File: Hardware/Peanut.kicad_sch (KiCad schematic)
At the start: 4 parts, among them J1 Conn_02x04_Odd_Even, J2 Conn_02x04_Odd_Even, SW6 Slide Switch

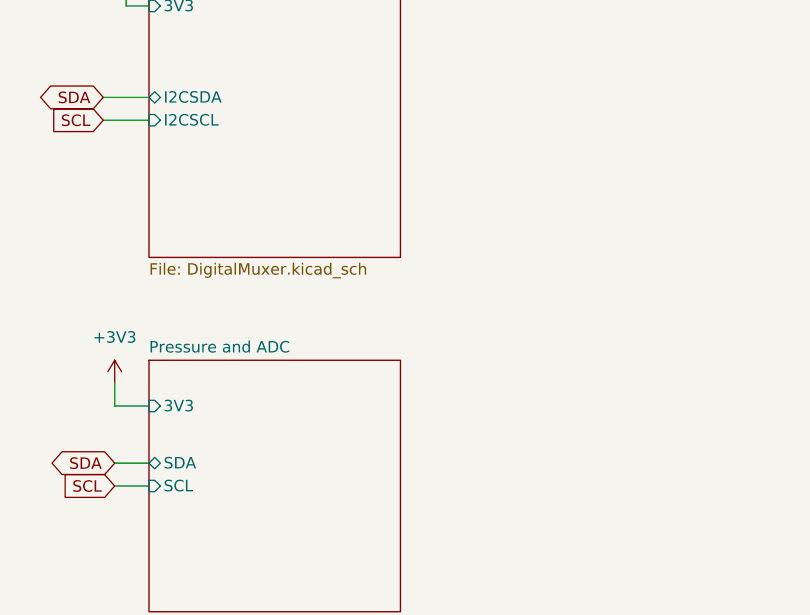
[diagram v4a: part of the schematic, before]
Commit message: Replace 1 LED with battery measurement toggle - We require an additional IO to toggle battery draining for % measurement, however we had no more ports. After a group discussion, one LED was dropped.
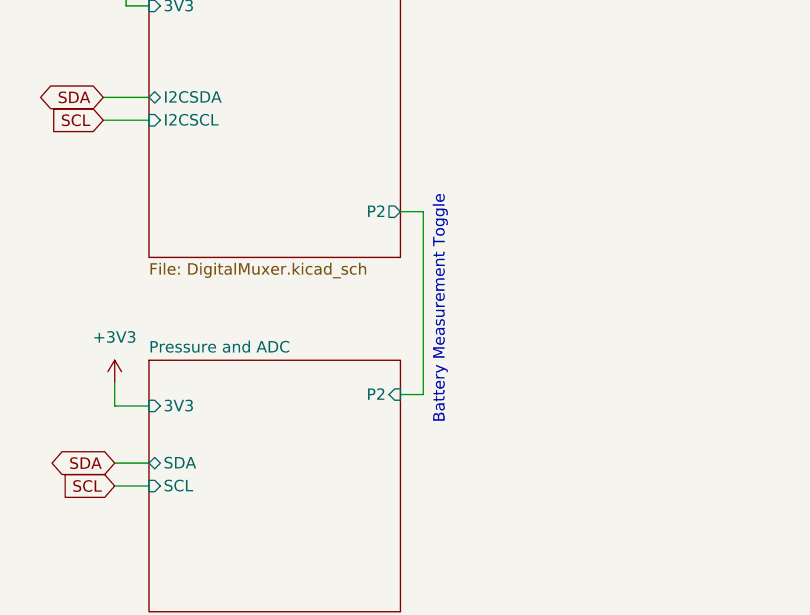
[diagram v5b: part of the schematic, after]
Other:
- sheet DigitalMuxer ports: added P2; removed none
- sheet Pressure and ADC ports: added P2; removed none
- note added: "Battery Measurement Toggle"
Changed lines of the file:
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@@
+	(wire
+		(pts
+			(xy 165.1 132.08) (xy 165.1 152.4)
+		)
+		(stroke
+			(width 0)
+			(type default)
+		)
+	)
 	(wire
 		(pts
@@
 	(wire
 		(pts
+			(xy 162.56 132.08) (xy 165.1 132.08)
+		)
+		(stroke
+			(width 0)
+			(type default)
+		)
+	)
+	(wire
+		(pts
 			(xy 175.26 38.1) (xy 177.8 38.1)
+		)
+		(stroke
+			(width 0)
+			(type default)
+		)
+	)
+	(wire
+		(pts
+			(xy 165.1 152.4) (xy 162.56 152.4)
 		)
 		(stroke
@@
 		(exclude_from_sim no)
 		(at 125.73 34.29 0)
+		(effects
+			(font
+				(size 1.27 1.27)
+			)
+		)
+	)
+	(text "Battery Measurement Toggle"
+		(exclude_from_sim no)
+		(at 166.878 143.002 90)
 		(effects
 			(font
@@
 			)
 		)
+		(pin "P2" output
+			(at 162.56 132.08 0)
+			(effects
+				(font
+					(size 1.27 1.27)
+				)
+				(justify right)
+			)
+		)
 		(instances
 			(project "Peanut"
@@
 			)
 		)
+		(pin "P2" input
+			(at 162.56 152.4 0)
+			(effects
+				(font
+					(size 1.27 1.27)
+				)
+				(justify right)
+			)
+		)

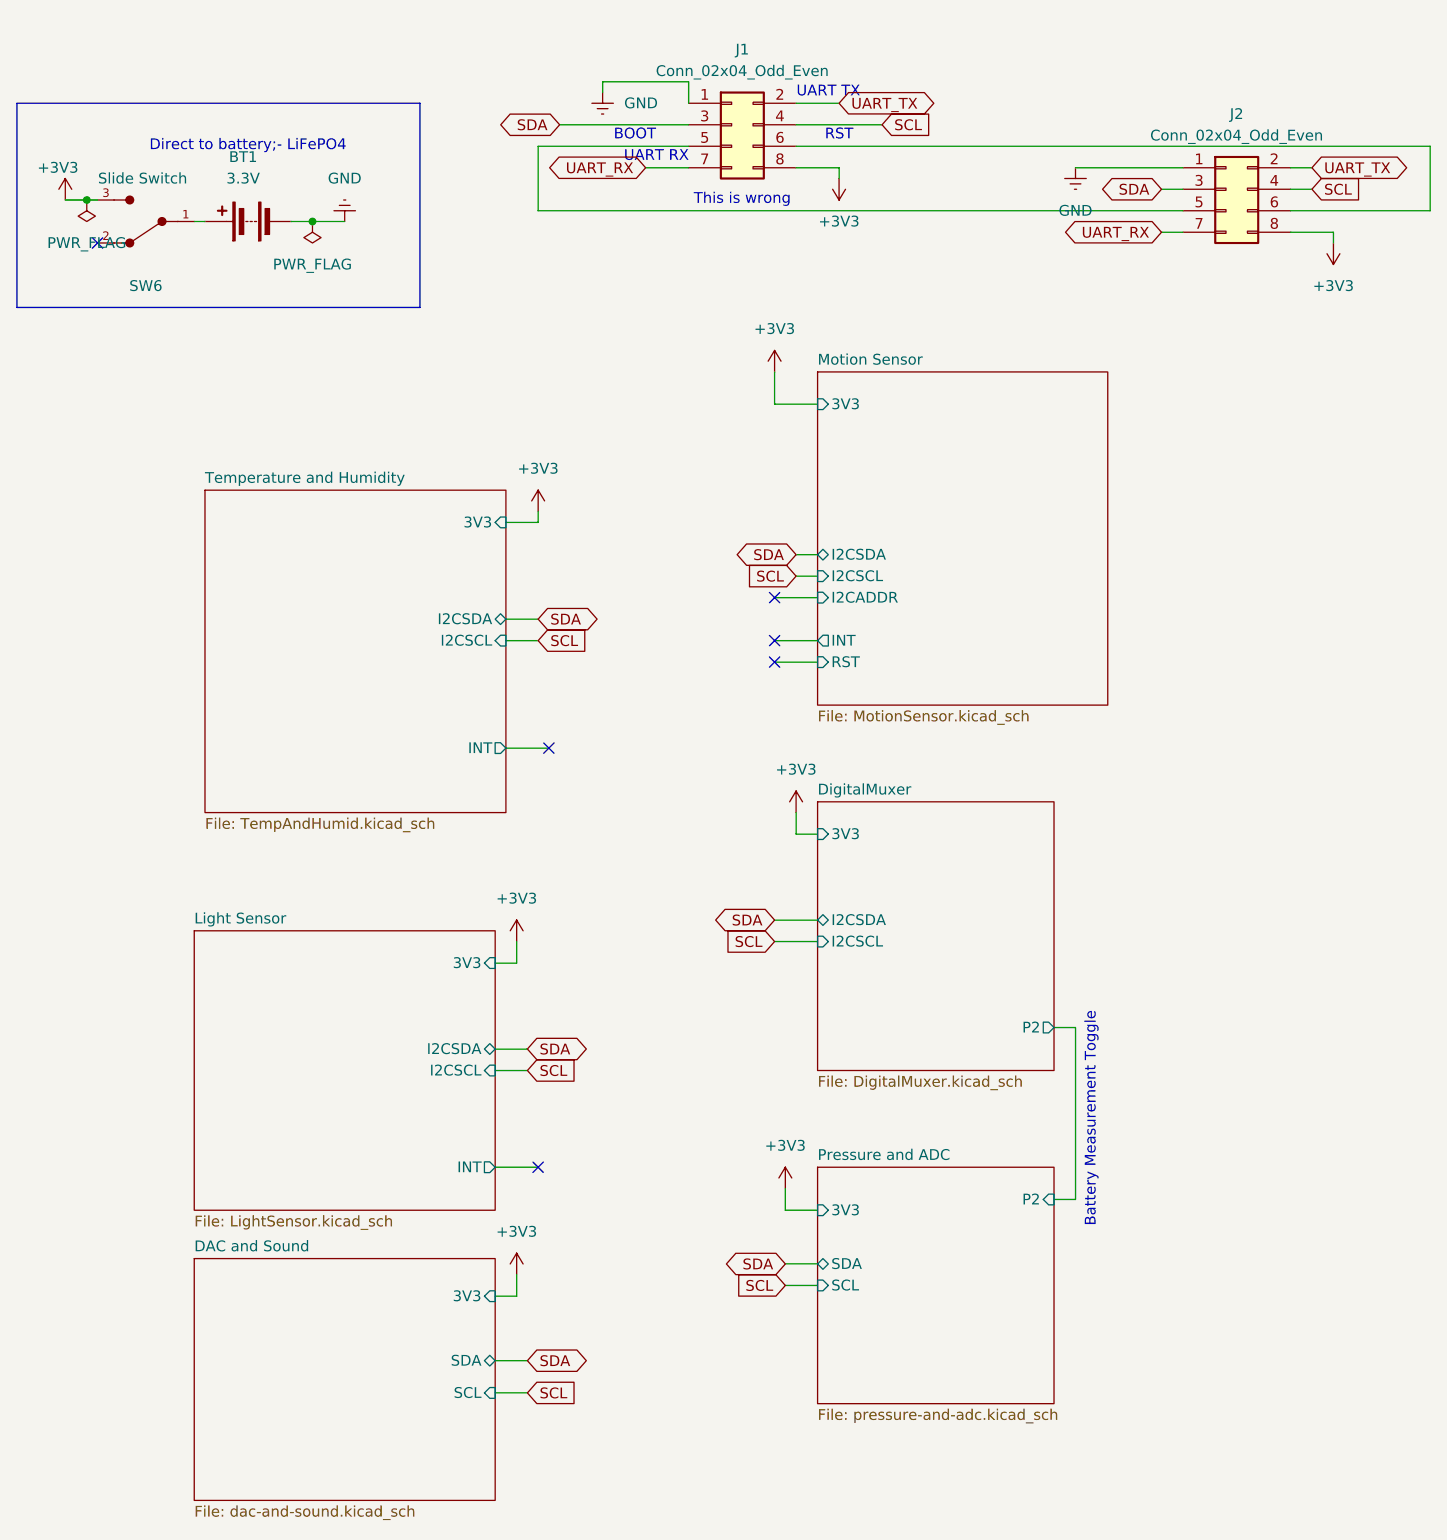
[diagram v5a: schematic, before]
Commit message: Add Battery Monitoring & Use Project Parts Library
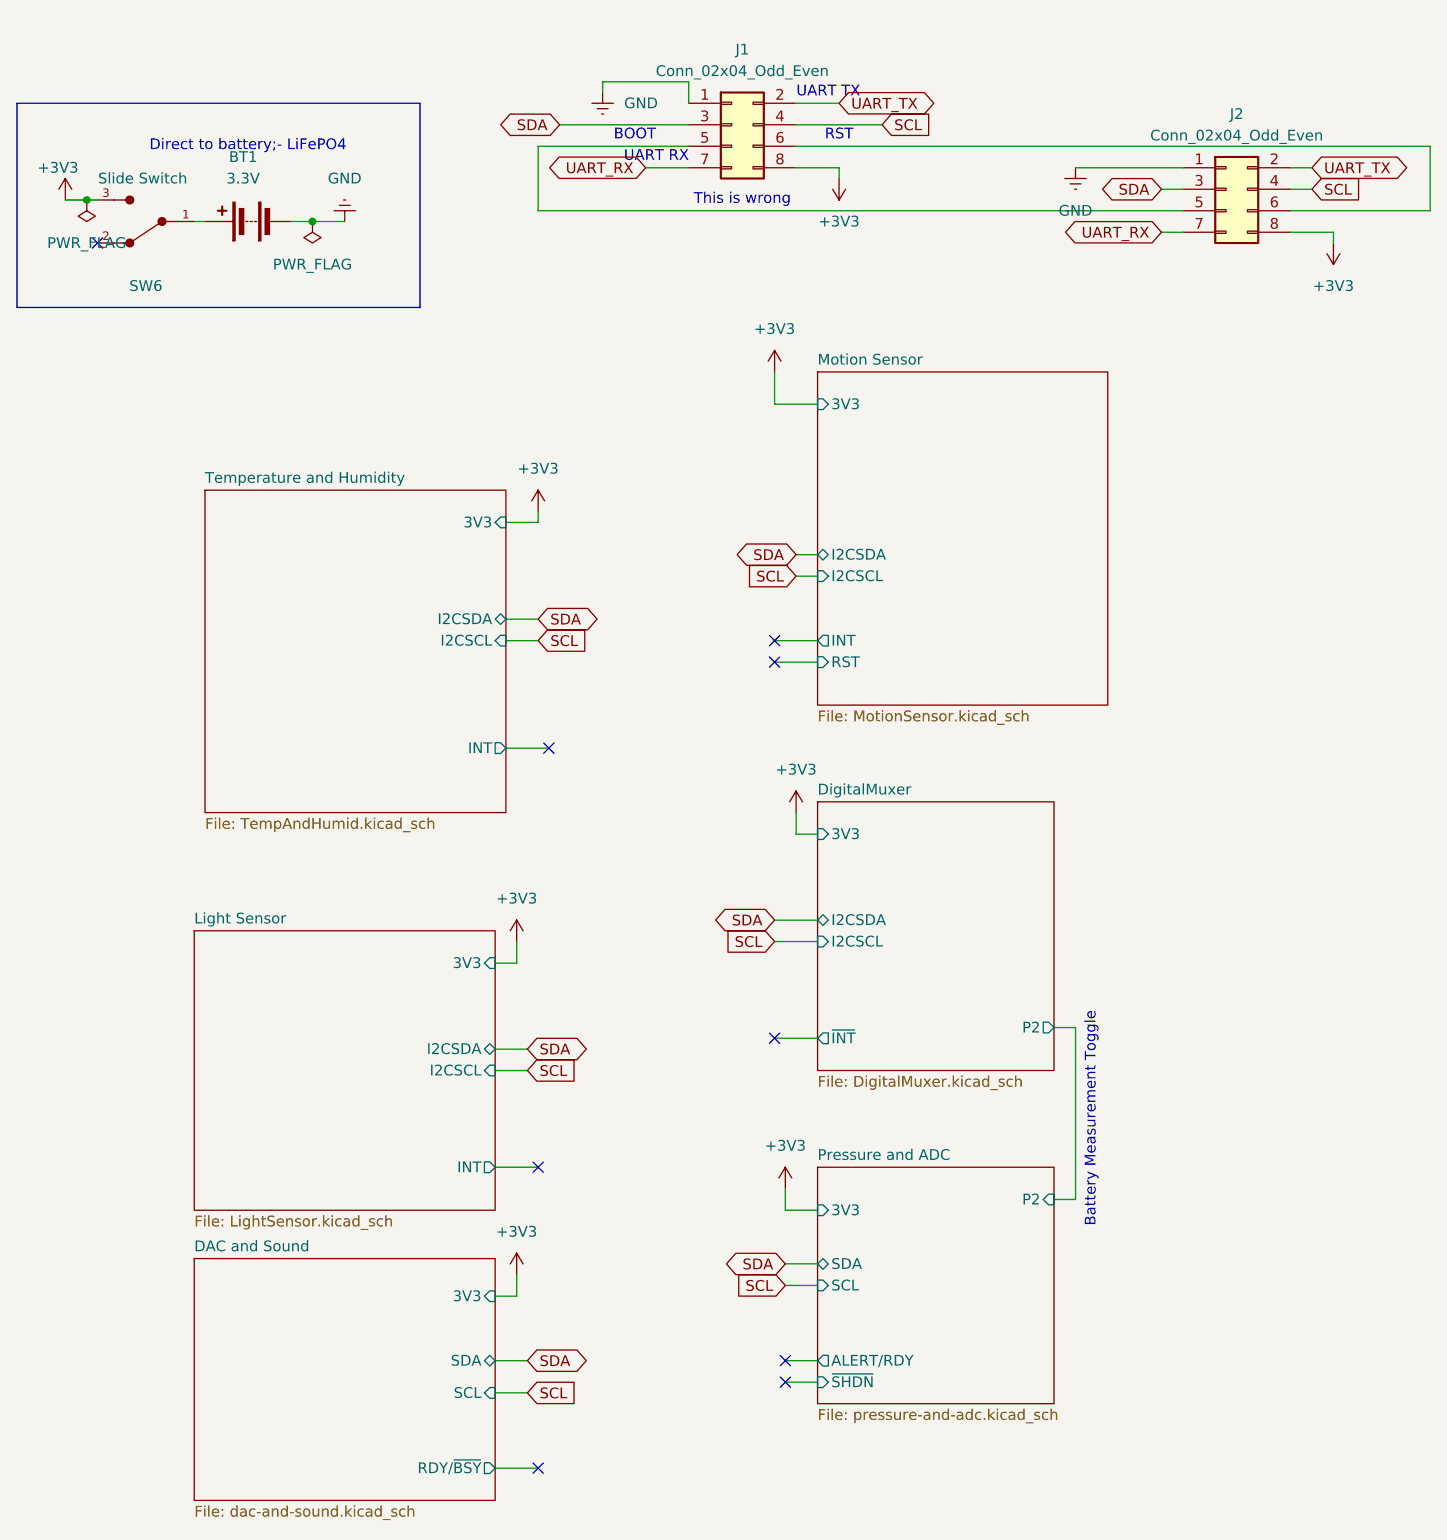
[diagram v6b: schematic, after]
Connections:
- no-connect marks 6 -> 9
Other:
- sheet DAC and Sound ports: added RDY/~{BSY}; removed none
- sheet DigitalMuxer ports: added ~{INT}; removed none
- sheet Motion Sensor ports: added none; removed I2CADDR
- sheet Pressure and ADC ports: added ALERT/RDY, ~{SHDN}; removed none
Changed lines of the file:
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@@
+	)
+	(no_connect
+		(at 130.81 171.45)
+	)
+	(no_connect
+		(at 129.54 133.35)
 	)
 	(no_connect
@@
 	)
 	(no_connect
+		(at 130.81 173.99)
+	)
+	(no_connect
 		(at 102.87 99.06)
+	)
+	(no_connect
+		(at 101.6 184.15)
 	)
 	(no_connect
 		(at 101.6 148.59)
 	)
-	(no_connect
-		(at 129.54 81.28)
-	)
 	(wire
 		(pts
@@
 	(wire
 		(pts
+			(xy 130.81 171.45) (xy 134.62 171.45)
+		)
+		(stroke
+			(width 0)
+			(type default)
+		)
+	)
+	(wire
+		(pts
 			(xy 193.04 30.48) (xy 190.5 30.48)
 		)
@@
 	(wire
 		(pts
+			(xy 96.52 184.15) (xy 101.6 184.15)
+		)
+		(stroke
+			(width 0)
+			(type default)
+		)
+	)
+	(wire
+		(pts
 			(xy 96.52 171.45) (xy 100.33 171.45)
 		)
@@
 	(wire
 		(pts
+			(xy 175.26 38.1) (xy 177.8 38.1)
+		)
+		(stroke
+			(width 0)
+			(type default)
+		)
+	)
+	(wire
+		(pts
+			(xy 129.54 133.35) (xy 134.62 133.35)
+		)
+		(stroke
+			(width 0)
+			(type default)
+		)
+	)
+	(wire
+		(pts
+			(xy 134.62 153.67) (xy 130.81 153.67)
+		)
+		(stroke
+			(width 0)
+			(type default)
+		)
+	)
+	(wire
+		(pts
+			(xy 132.08 25.4) (xy 142.24 25.4)
+		)
+		(stroke
+			(width 0)
+			(type default)
+		)
+	)
+	(wire
+		(pts
+			(xy 130.81 173.99) (xy 134.62 173.99)
+		)
+		(stroke
+			(width 0)
+			(type default)
+		)
+	)
+	(wire
+		(pts
+			(xy 109.22 20.32) (xy 119.38 20.32)
+		)
+		(stroke
+			(width 0)
+			(type default)
+		)
+	)
+	(wire
+		(pts
 			(xy 162.56 132.08) (xy 165.1 132.08)
 		)
@@
 	(wire
 		(pts
-			(xy 175.26 38.1) (xy 177.8 38.1)
-		)
-		(stroke
-			(width 0)
-			(type default)
-		)
-	)
-	(wire
-		(pts
-			(xy 165.1 152.4) (xy 162.56 152.4)
-		)
-		(stroke
-			(width 0)
-			(type default)
-		)
-	)
-	(wire
-		(pts
-			(xy 134.62 153.67) (xy 130.81 153.67)
-		)
-		(stroke
-			(width 0)
-			(type default)
-		)
-	)
-	(wire
-		(pts
-			(xy 132.08 25.4) (xy 142.24 25.4)
-		)
-		(stroke
-			(width 0)
-			(type default)
-		)
-	)
-	(wire
-		(pts
-			(xy 109.22 20.32) (xy 119.38 20.32)
-		)
-		(stroke
-			(width 0)
-			(type default)
-		)
-	)
-	(wire
-		(pts
 			(xy 175.26 33.02) (xy 177.8 33.02)
 		)
@@
 	(wire
 		(pts
+			(xy 162.56 152.4) (xy 165.1 152.4)
+		)
+		(stroke
+			(width 0)
+			(type default)
+		)
+	)
+	(wire
+		(pts
 			(xy 96.52 134.62) (xy 100.33 134.62)
 		)
@@
 		(pts
 			(xy 99.06 161.29) (xy 99.06 163.83)
-		)
-		(stroke
-			(width 0)
-			(type default)
-		)
-	)
-	(wire
-		(pts
-			(xy 129.54 81.28) (xy 134.62 81.28)
 		)
 		(stroke
@@
 			)
 		)
-		(property "Description" "SPDT Slide Switch with 10mm length, 5mm width and 10mm hight."
+		(property "Description" "SPDT Slide Switch"
 			(at 54.61 36.83 0)
 			(effects
@@
 			)
 		)
+		(pin "~{INT}" output
+			(at 134.62 133.35 180)
+			(effects
+				(font
+					(size 1.27 1.27)
+				)
+				(justify left)
+			)
+		)
 		(instances
 			(project "Peanut"
@@
 			)
 		)
+		(pin "ALERT{slash}RDY" output
+			(at 134.62 171.45 180)
+			(effects
+				(font
+					(size 1.27 1.27)
+				)
+				(justify left)
+			)
+		)
+		(pin "~{SHDN}" input
+			(at 134.62 173.99 180)
+			(effects
+				(font
+					(size 1.27 1.27)
+				)
+				(justify left)
+			)
+		)
 		(instances
 			(project "Peanut"
@@
 			)
 		)
-		(pin "I2CADDR" input
-			(at 134.62 81.28 180)
-			(effects
-				(font
-					(size 1.27 1.27)
-				)
-				(justify left)
-			)
-		)
 		(pin "RST" input
 			(at 134.62 88.9 180)
@@
 			(effects
 				(font
+					(size 1.27 1.27)
+				)
+				(justify right)
+			)
+		)
+		(pin "RDY{slash}~{BSY}" output
+			(at 96.52 184.15 0)
+			(effects
+				(font

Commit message: Fully wired board!
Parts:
- SW6: footprint Button_Switch_THT:SW_E-Switch_EG1224_SPDT_Angled -> Peanut:SW-TH_SK12D07VG4
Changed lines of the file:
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@@
 			)
 		)
-		(property "Footprint" "Button_Switch_THT:SW_E-Switch_EG1224_SPDT_Angled"
+		(property "Footprint" "Peanut:SW-TH_SK12D07VG4"
 			(at 53.34 29.21 0)
 			(effects

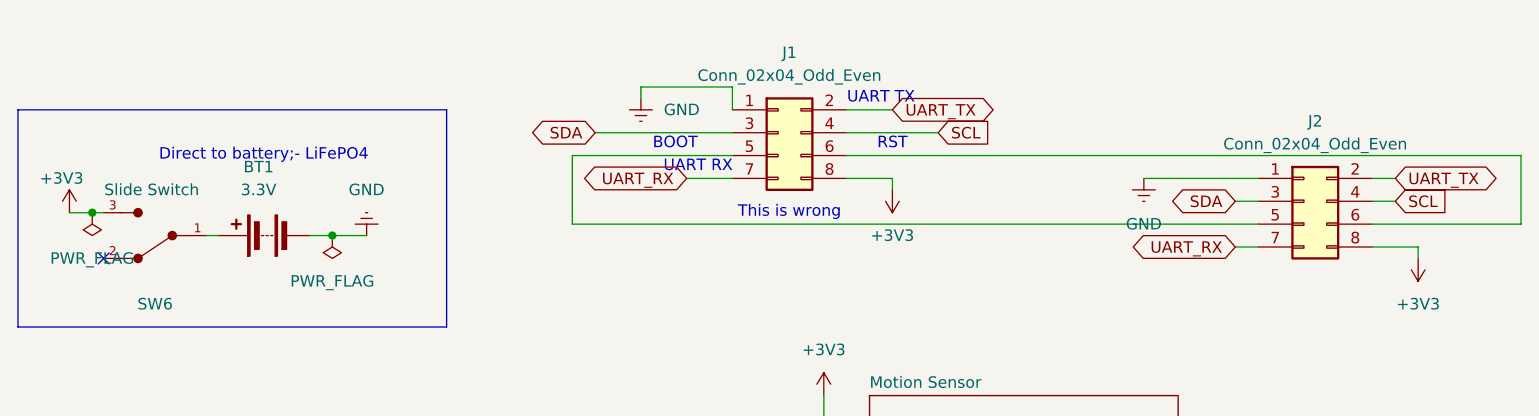
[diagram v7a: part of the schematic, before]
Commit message: Initial OS architecture, and updated PCB work After a joint planning session, designed and architected OS structure: ``` src/ |- os: Audio, Accelerometer, Humidity, etc |- drivers: I2C interfaces, per-chip ```
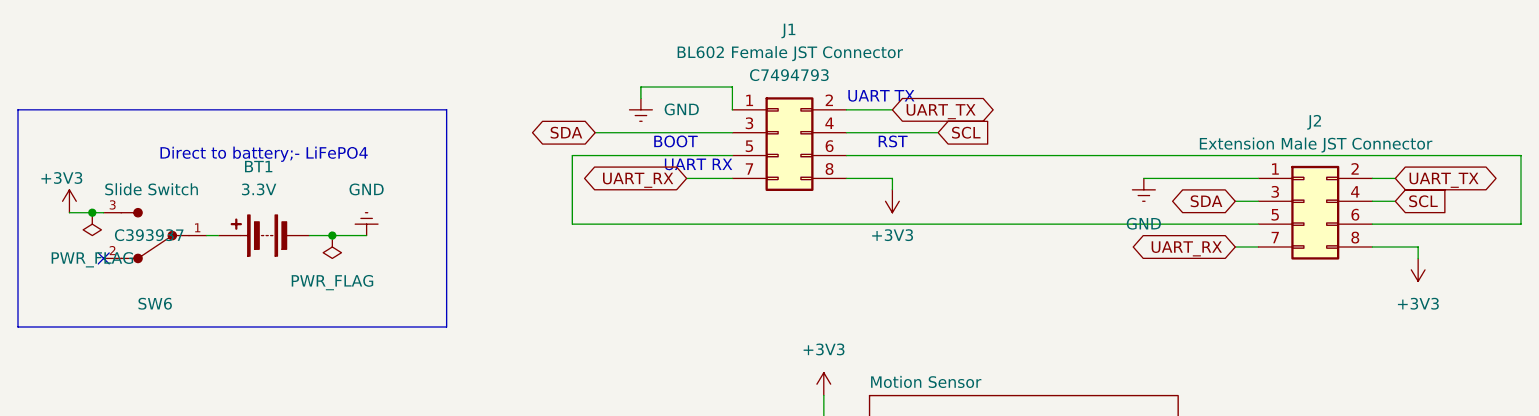
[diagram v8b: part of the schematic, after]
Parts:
- J1: value Conn_02x04_Odd_Even -> BL602 Female JST Connector; symbol Connector_Generic:Conn_02x04_Odd_Even -> Peanut:bl602 Connector; LCSC (none) -> C7494793
- J2: value Conn_02x04_Odd_Even -> Extension Male JST Connector; footprint Connector_PinHeader_2.54mm:PinHeader_2x04_P2.54mm_Horizontal -> Peanut:PinHeader_2x04_P2.54mm_Horizontal_Flipped
- SW6: LCSC (none) -> C393937
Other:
- note removed: "This is wrong"
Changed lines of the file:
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@@
-		)
-	)
-	(text "This is wrong"
-		(exclude_from_sim no)
-		(at 125.73 34.29 0)
-		(effects
-			(font
-				(size 1.27 1.27)
-			)
 		)
 	)
@@
 			)
 		)
+		(property "LCSC" "C393937"
+			(at 54.61 36.83 0)
+			(effects
+				(font
+					(size 1.27 1.27)
+				)
+			)
+		)
 		(pin "3"
 		)
@@
 			)
 		)
-		(property "Value" "Conn_02x04_Odd_Even"
+		(property "Value" "Extension Male JST Connector"
 			(at 184.15 26.67 0)
 			(effects
@@
 			)
 		)
-		(property "Footprint" "Connector_PinHeader_2.54mm:PinHeader_2x04_P2.54mm_Horizontal"
+		(property "Footprint" "Peanut:PinHeader_2x04_P2.54mm_Horizontal_Flipped"
 			(at 182.88 33.02 0)
 			(effects
@@
 	)
 	(symbol
-		(lib_id "Connector_Generic:Conn_02x04_Odd_Even")
+		(lib_id "Peanut:bl602 Connector")
 		(at 124.46 25.4 0)
 		(unit 1)
@@
 		(fields_autoplaced yes)
 		(property "Reference" "J1"
+			(at 125.73 13.97 0)
+			(effects
+				(font
+					(size 1.27 1.27)
+				)
+			)
+		)
+		(property "Value" "BL602 Female JST Connector"
 			(at 125.73 16.51 0)
-			(effects
-				(font
-					(size 1.27 1.27)
-				)
-			)
-		)
-		(property "Value" "Conn_02x04_Odd_Even"
-			(at 125.73 19.05 0)
 			(effects
 				(font
@@
 			)
 		)
+		(property "LCSC" "C7494793"
+			(at 125.73 19.05 0)
+			(effects
+				(font
+					(size 1.27 1.27)
+				)
+			)
+		)
